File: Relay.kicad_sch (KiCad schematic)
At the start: 24 parts, among them J40 Screw_Terminal_01x02, K1 HF46F-G/012-HS1T, K2 T9AS1D12-12, K3 HF46F-G/012-HS1T, K4 HF46F-G/012-HS1T, Q1 BSS806, Q2 BSS806

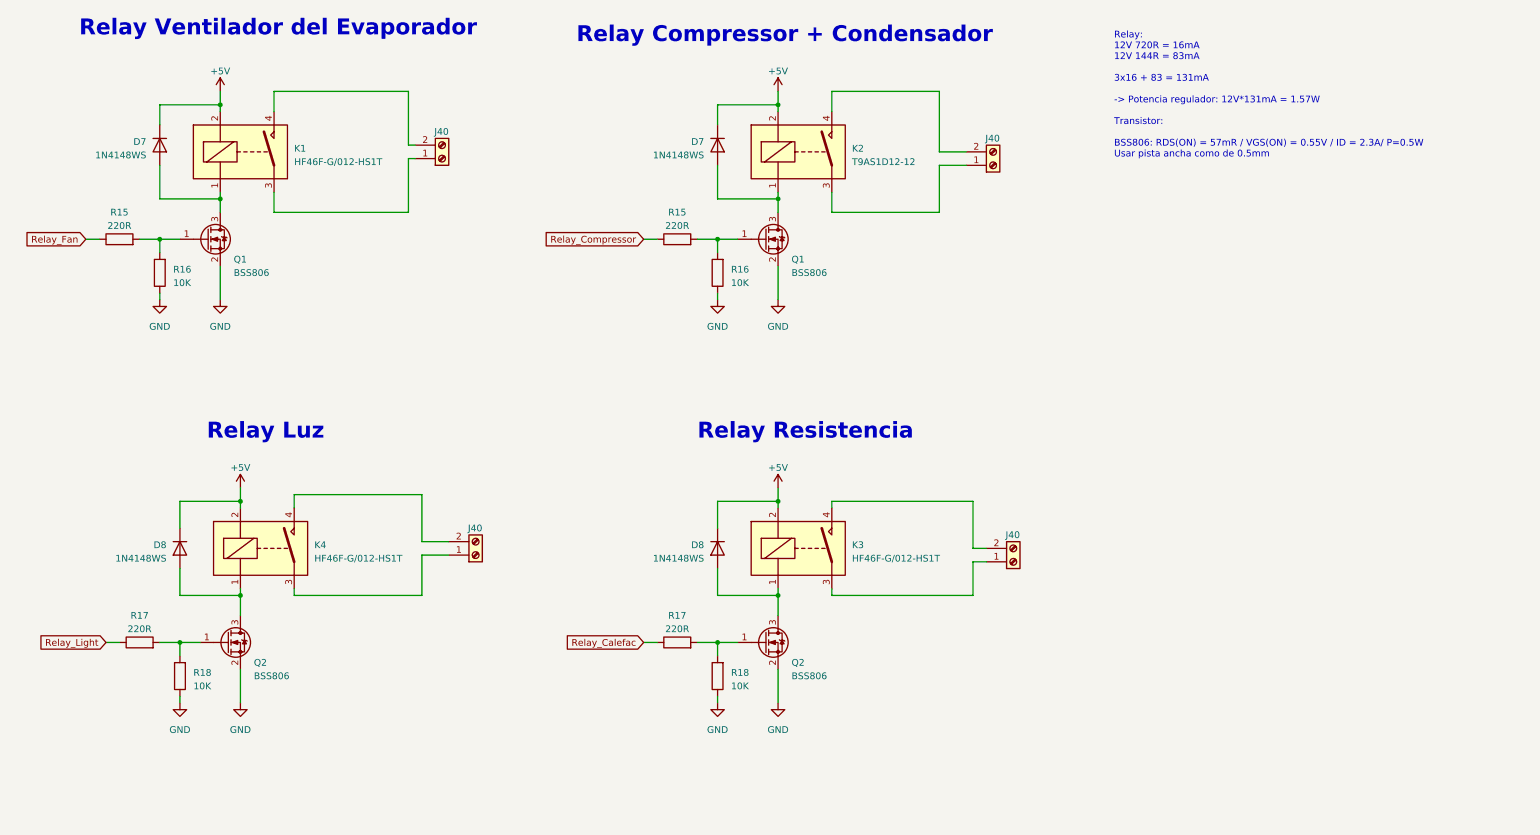
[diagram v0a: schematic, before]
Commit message: SCH: Se cambió el IRM, se colocó filtro en la entrada AC, se modificó la fuente switching LM, se corrigieron algunos errores de diseño. PCB: Se terminó el placement de los componentes
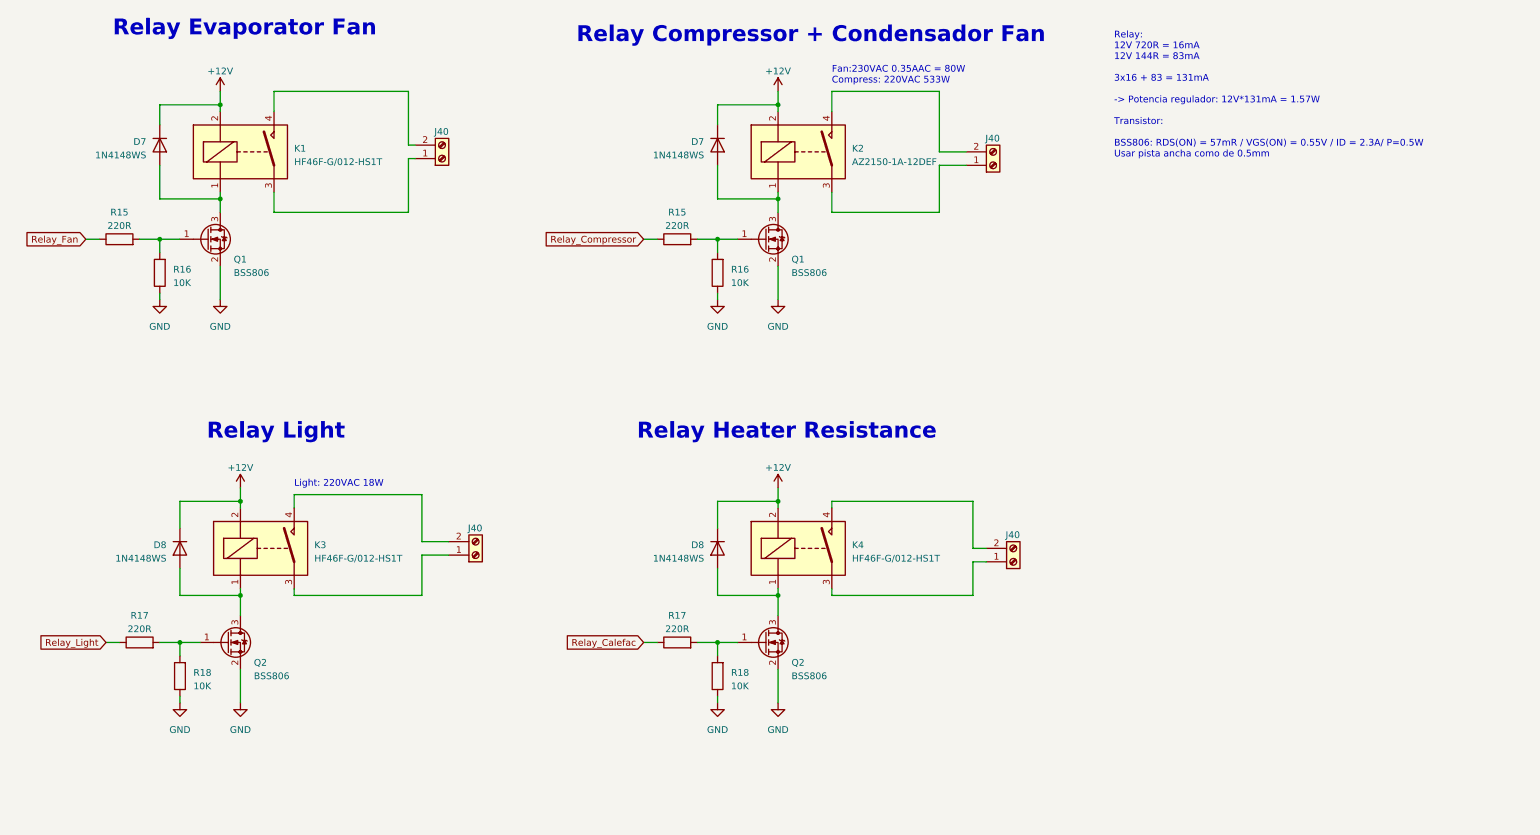
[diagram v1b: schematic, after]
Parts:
- K2: value T9AS1D12-12 -> AZ2150-1A-12DEF; footprint 1-Relay:Relay_TE-Connectivity_SPST-NO_32.5x27.4x27.9mm -> 1-Relay:Relay_Zettler_SPST-NO_31.8x26.9x19.1mm
- renumbered K4 to K3, K3 to K4
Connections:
- net +5V renamed +12V
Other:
- note added: "Fan:230VAC 0.35AAC = 80W Compress: 220VAC 533W"
- note added: "Light: 220VAC 18W"
- note added: "Relay Compressor + Condensador Fan"
- note added: "Relay Evaporator Fan"
- note added: "Relay Heater Resistance"
- note added: "Relay Light"
- note removed: "Relay Compressor + Condensador"
- note removed: "Relay Luz"
- note removed: "Relay Resistencia"
- note removed: "Relay Ventilador del Evaporador"

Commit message: Se guarda avance
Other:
- note added: "220VAC 100R"
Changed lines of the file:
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@@
     (effects (font (size 3 3) (thickness 0.6) bold) (justify left bottom))
+  )
+  (text "220VAC 100R" (at 165.1 111.76 0)
+    (effects (font (size 1.27 1.27)) (justify left bottom))
   )
   (text "Relay Light" (at 46.99 101.6 0)

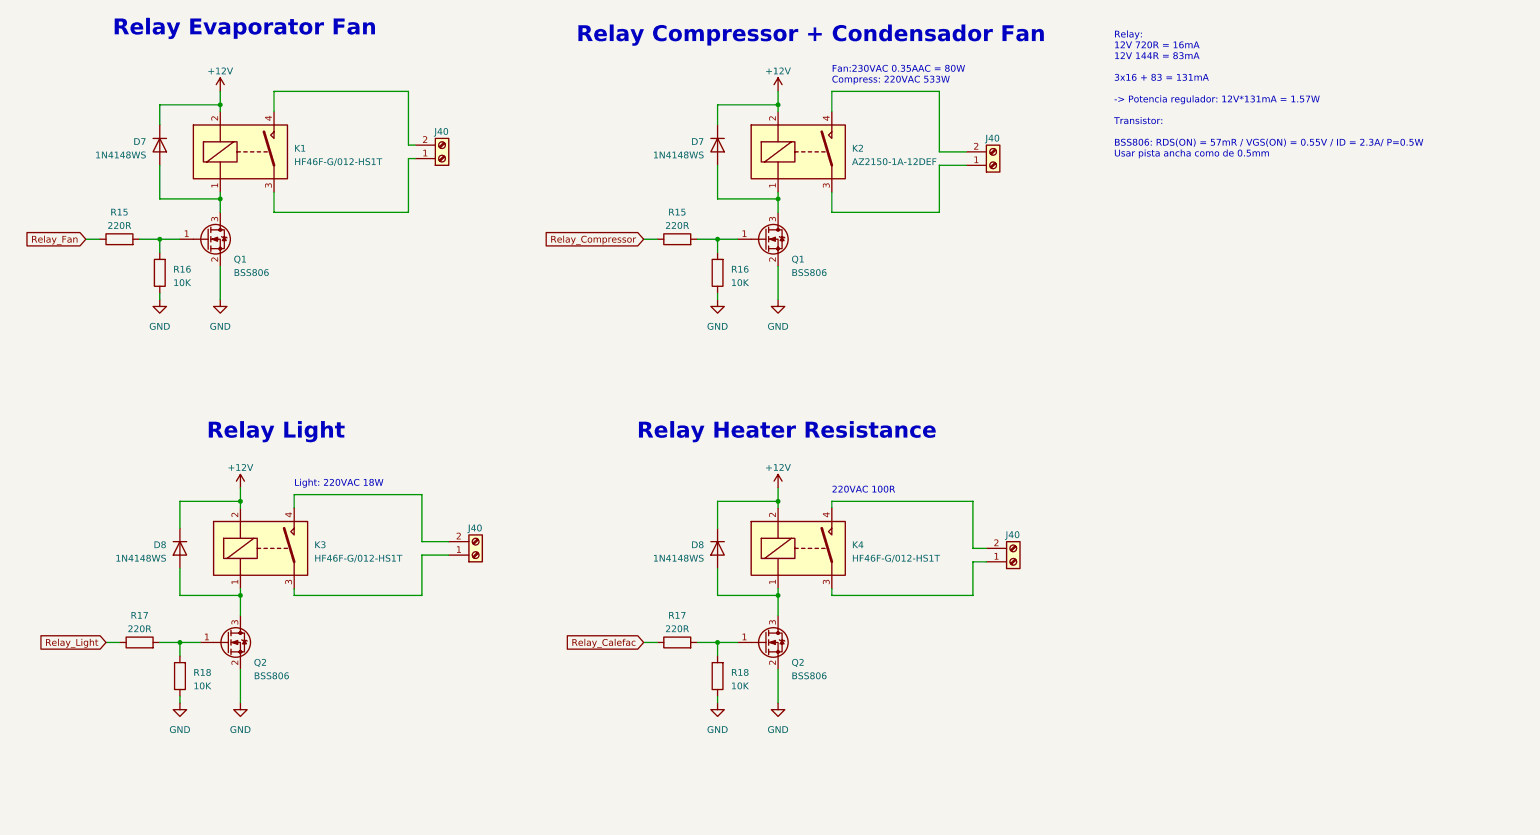
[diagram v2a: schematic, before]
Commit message: SCH: Se cambian la bornera por terminales, se añade un disparo más para el compressor (falta conectarlo al uC), falta modificar, se cambia la fuente switching por otra de menos costo
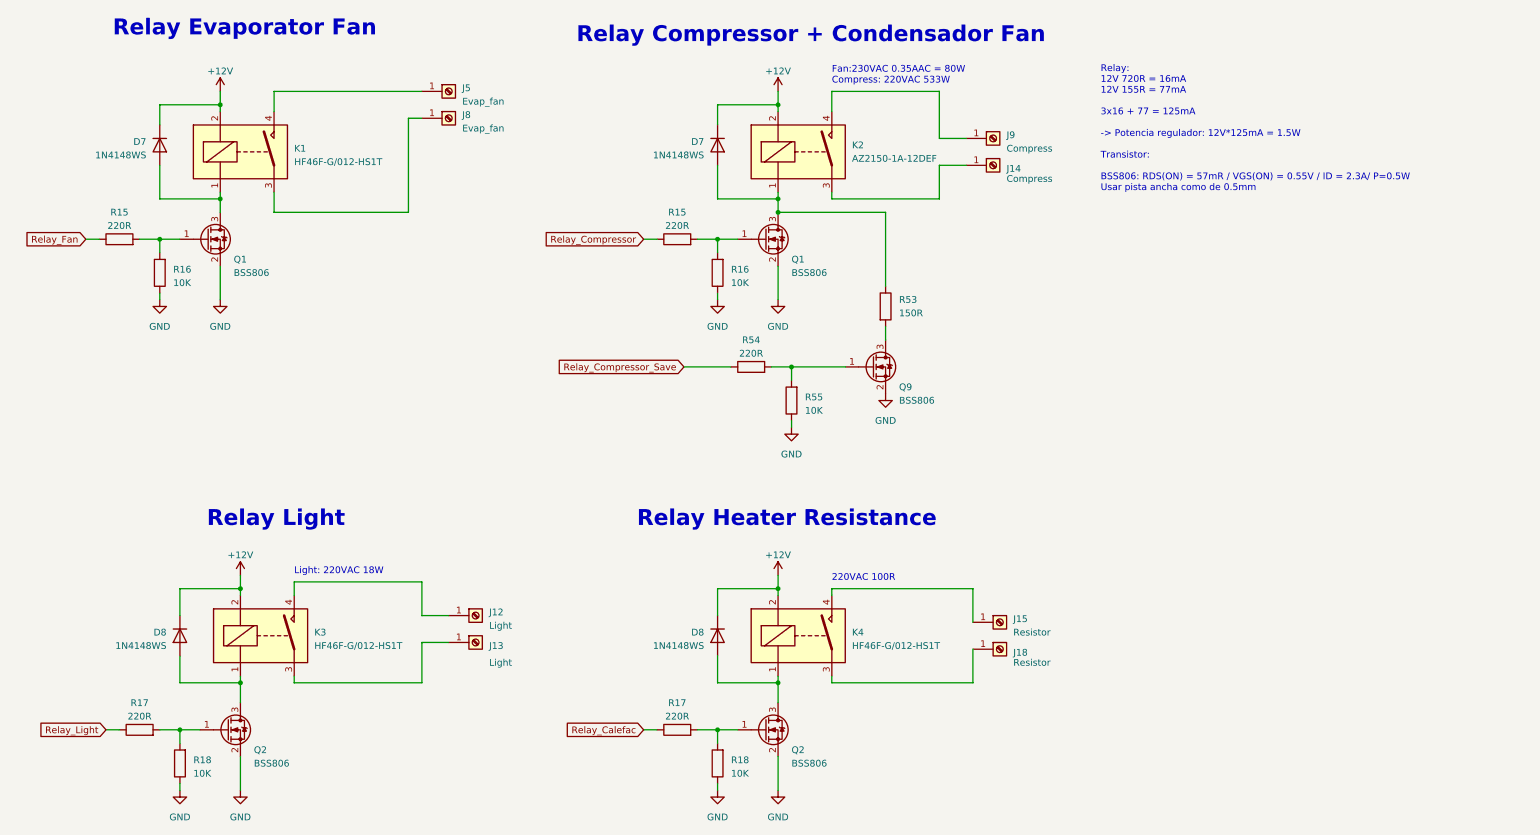
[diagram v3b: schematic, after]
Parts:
- removed J40 (x4): Screw_Terminal_01x02, 1-Terminal-Block:DG504-5.08-02P_or_SMKDS 2,5-2-5.08, symbol 1-Terminal-Block:DG504-5.08-02P
- added J12, J13: Light, 1-Pad:Solder-Terminal_FS1536_6.3x0.8mm_NINIGI, symbol Connector:Screw_Terminal_01x01
- added J14, J9: Compress, 1-Pad:Solder-Terminal_FS1536_6.3x0.8mm_NINIGI, symbol Connector:Screw_Terminal_01x01
- added J15, J18: Resistor, 1-Pad:Solder-Terminal_FS1536_6.3x0.8mm_NINIGI, symbol Connector:Screw_Terminal_01x01
- added J5, J8: Evap_fan, 1-Pad:Solder-Terminal_FS1536_6.3x0.8mm_NINIGI, symbol Connector:Screw_Terminal_01x01
- added Q9: BSS806, Package_TO_SOT_SMD:SOT-23, symbol Transistor_FET:BSS123
- added R53: 150R, 1-Resistor:R_2512_6332Metric, symbol 1-Resistor:R_2512
- added R54: 220R, 1-Resistor:R_0805_2012Metric, symbol 1-Resistor:R_0805
- added R55: 10K, 1-Resistor:R_0805_2012Metric, symbol 1-Resistor:R_0805
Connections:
- net GND: now also Q9.2 (S), R55.1
- net at K1.3: now also J8.1 (Pin_1)
- net at K1.4: now also J5.1 (Pin_1)
- net at D7.2 (A), K2.1, Q1.3 (D): now also R53.1
- net at K2.3: now also J14.1 (Pin_1)
- net at K2.4: now also J9.1 (Pin_1)
- net at K3.3: now also J13.1 (Pin_1)
- net at K3.4: now also J12.1 (Pin_1)
- net at K4.3: now also J18.1 (Pin_1)
- net at K4.4: now also J15.1 (Pin_1)
- new net: Q9.1 (G), R54.2, R55.2
- new net: Q9.3 (D), R53.2
- new net Relay_Compressor_Save: R54.1
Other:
- note added: "Relay: 12V 720R = 16mA 12V 155R = 77mA 3x16 + 77 = 125mA -> Potencia regulador: 12V*125mA = 1.5W Transistor: BSS806: RDS(ON) = 57mR / VGS(ON) = 0.55V / ID = 2.3A/ P=0.5W Usar pista ancha como de 0.5mm"
- note removed: "Relay: 12V 720R = 16mA 12V 144R = 83mA 3x16 + 83 = 131mA -> Potencia regulador: 12V*131mA = 1.57W Transistor: BSS806: RDS(ON) = 57mR / VGS(ON) = 0.55V / ID = 2.3A/ P=0.5W Usar pista ancha como de 0.5mm"
- moved on the sheet: D8, K3, K4, Q2, R17, R18
